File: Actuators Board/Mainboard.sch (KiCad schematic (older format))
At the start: 41 parts, among them J10 Conn_01x02_Male, J9 Conn_01x02_Male, Q1 MMDT2222A, U1 CP2102N-A01-GQFN24, U2 SN65HVD230, U3 ESP32-WROOM-32D

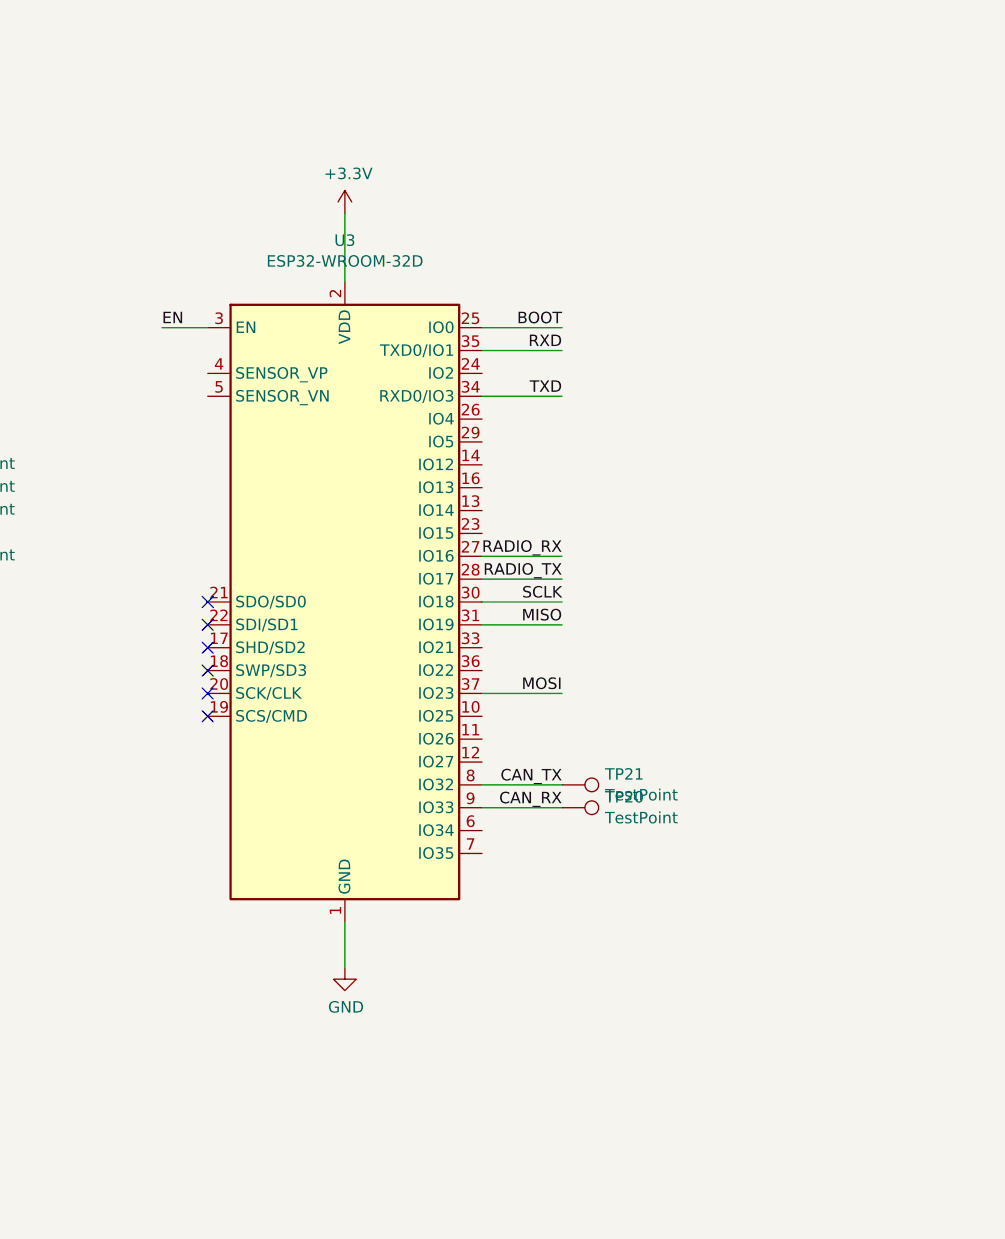
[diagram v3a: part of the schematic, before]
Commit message: pico swap done
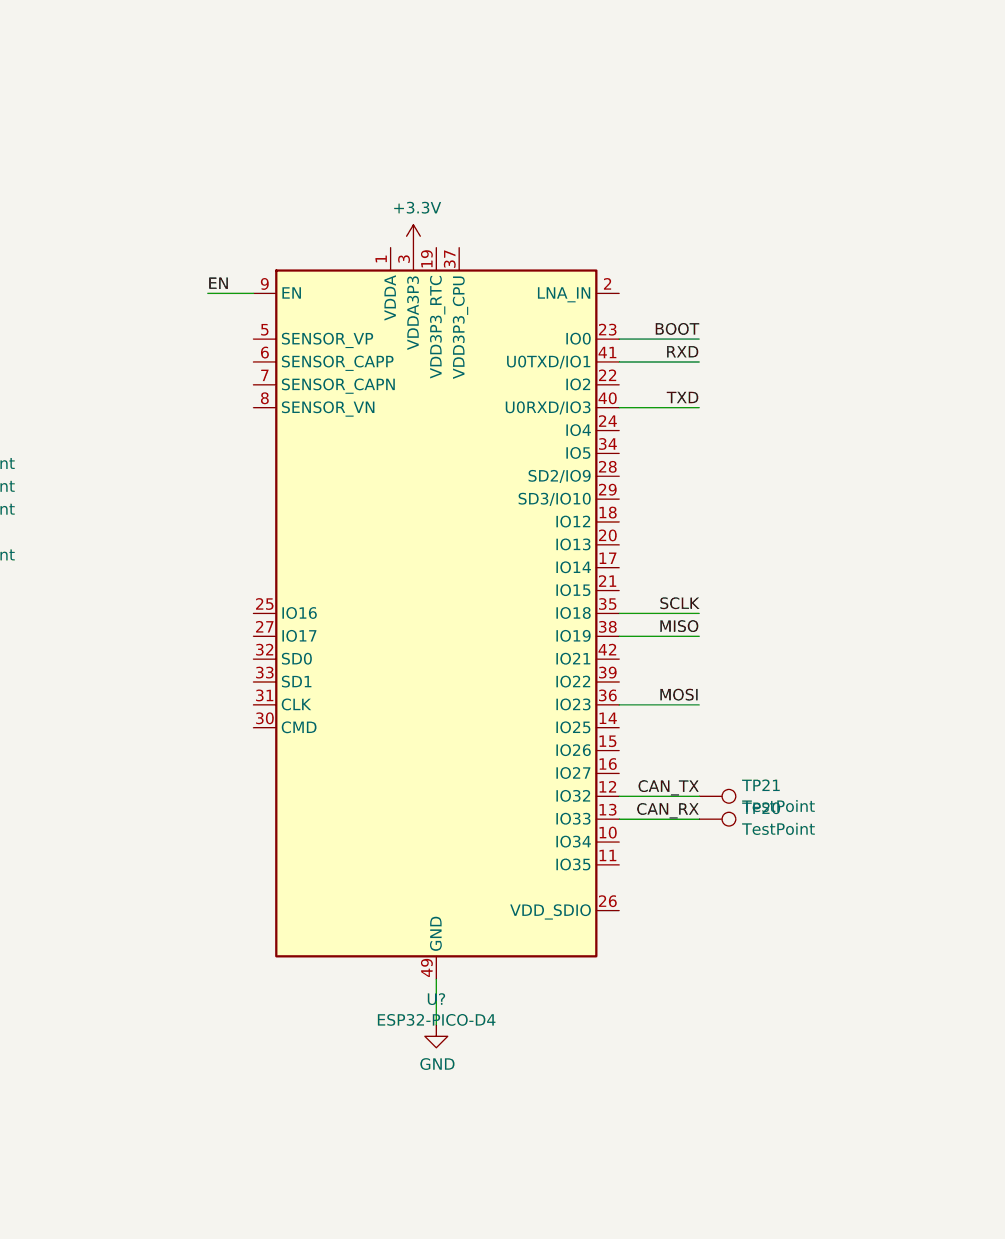
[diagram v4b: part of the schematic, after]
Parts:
- removed U3: ESP32-WROOM-32D, RF_Module:ESP32-WROOM-32, symbol RF_Module:ESP32-WROOM-32
- added U?: ESP32-PICO-D4, Package_DFN_QFN:QFN-48-1EP_7x7mm_P0.5mm_EP5.3x5.3mm, symbol RF_Module:ESP32-PICO-D4
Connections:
- net +3V3: now also U?.3 (VDDA3P3), U?.4 (VDDA3P3)
- net BOOT: now also U?.23 (IO0)
- net CAN_RX: now also U?.13 (IO33)
- net CAN_TX: now also U?.12 (IO32)
- net EN: now also U?.9 (EN)
- net GND: now also U?.49 (GND)
- net MISO: now also U?.38 (IO19)
- net MOSI: now also U?.36 (IO23)
- net RXD: now also U?.41 (U0TXD/IO1)
- net SCLK: now also U?.35 (IO18)
- net TXD: now also U?.40 (U0RXD/IO3)
- new net: U?.1 (VDDA), U?.43 (VDDA), U?.46 (VDDA)
- no-connect marks 19 -> 13
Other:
- moved on the sheet: TP20, TP21
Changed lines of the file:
@@
 L power:+3.3V #PWR020
 U 1 1 5DA60792
-P 6250 2050
-F 0 "#PWR020" H 6250 1900 50  0001 C CNN
-F 1 "+3.3V" H 6265 2223 50  0000 C CNN
-F 2 "" H 6250 2050 50  0001 C CNN
-F 3 "" H 6250 2050 50  0001 C CNN
-	1    6250 2050
-	1    0    0    -1
-$EndComp
-Wire Wire Line
-	6250 2050 6250 2350
+P 6550 2200
+F 0 "#PWR020" H 6550 2050 50  0001 C CNN
+F 1 "+3.3V" H 6565 2373 50  0000 C CNN
+F 2 "" H 6550 2200 50  0001 C CNN
+F 3 "" H 6550 2200 50  0001 C CNN
+	1    6550 2200
+	1    0    0    -1
+$EndComp
 $Comp
 L power:GND #PWR021
 U 1 1 5DA6110D
-P 6250 5350
-F 0 "#PWR021" H 6250 5100 50  0001 C CNN
-F 1 "GND" H 6255 5177 50  0000 C CNN
-F 2 "" H 6250 5350 50  0001 C CNN
-F 3 "" H 6250 5350 50  0001 C CNN
-	1    6250 5350
-	1    0    0    -1
-$EndComp
-Wire Wire Line
-	6250 5150 6250 5350
+P 6650 5600
+F 0 "#PWR021" H 6650 5350 50  0001 C CNN
+F 1 "GND" H 6655 5427 50  0000 C CNN
+F 2 "" H 6650 5600 50  0001 C CNN
+F 3 "" H 6650 5600 50  0001 C CNN
+	1    6650 5600
+	1    0    0    -1
+$EndComp
+Wire Wire Line
+	6650 5400 6650 5600
 $Comp
 L power:+3.3V #PWR06
@@
 Text Notes 10600 7700 0    50   ~ 0
 0.1\n\n
-Text Label 7200 3850 2    50   ~ 0
+Text Label 7800 3900 2    50   ~ 0
 MISO
-Text Label 7200 3750 2    50   ~ 0
+Text Label 7800 3800 2    50   ~ 0
 SCLK
-Wire Wire Line
-	5450 2550 5650 2550
-Text Label 5450 2550 0    50   ~ 0
-EN
 Text Label 1550 7550 2    50   ~ 0
 EN
-Text Label 7200 2550 2    50   ~ 0
+Text Label 7800 2600 2    50   ~ 0
 BOOT
 $Comp
@@
 TXD
 Wire Wire Line
-	6850 2550 7200 2550
-Wire Wire Line
-	6850 2650 7200 2650
-Wire Wire Line
-	6850 2850 7200 2850
-Wire Wire Line
-	6850 3750 7200 3750
-Wire Wire Line
-	6850 3850 7200 3850
-Wire Wire Line
-	6850 4150 7200 4150
+	7450 2600 7800 2600
+Wire Wire Line
+	7450 2700 7800 2700
+Wire Wire Line
+	7450 2900 7800 2900
+Wire Wire Line
+	7450 3800 7800 3800
+Wire Wire Line
+	7450 3900 7800 3900
+Wire Wire Line
+	7450 4200 7800 4200
 NoConn ~ 4000 3800
 NoConn ~ 4000 3900
@@
 Text Label 4300 3300 2    50   ~ 0
 TXD
-Text Label 7200 2650 2    50   ~ 0
+Text Label 7800 2700 2    50   ~ 0
 RXD
-Text Label 7200 2850 2    50   ~ 0
+Text Label 7800 2900 2    50   ~ 0
 TXD
 $Comp
@@
 	2200 2750 2400 2750
 Wire Wire Line
-	6850 3650 7200 3650
-Wire Wire Line
-	6850 3550 7200 3550
-Text Label 7200 3550 2    50   ~ 0
-RADIO_RX
-Text Label 7200 3650 2    50   ~ 0
-RADIO_TX
-$Comp
-L RF_Module:ESP32-WROOM-32 U3
-U 1 1 5DA5F4C7
-P 6250 3750
-F 0 "U3" H 6250 5331 50  0000 C CNN
-F 1 "ESP32-WROOM-32D" H 6250 5240 50  0000 C CNN
-F 2 "RF_Module:ESP32-WROOM-32" H 6250 2250 50  0001 C CNN
-F 3 "https://www.espressif.com/sites/default/files/documentation/esp32-wroom-32d_esp32-wroom-32u_datasheet_en.pdf" H 5950 3800 50  0001 C CNN
-	1    6250 3750
-	1    0    0    -1
-$EndComp
-Wire Wire Line
-	6850 4650 7200 4650
-Wire Wire Line
-	6850 4550 7200 4550
-Text Label 7200 4650 2    50   ~ 0
+	7450 4700 7800 4700
+Wire Wire Line
+	7450 4600 7800 4600
+Text Label 7800 4700 2    50   ~ 0
 CAN_RX
-Text Label 7200 4550 2    50   ~ 0
+Text Label 7800 4600 2    50   ~ 0
 CAN_TX
 Wire Wire Line
@@
 Wire Wire Line
 	3850 7050 4150 7050
-Text Label 7200 4150 2    50   ~ 0
+Text Label 7800 4200 2    50   ~ 0
 MOSI
 Wire Wire Line
@@
 L Connector:TestPoint TP20
 U 1 1 5DF4B310
-P 7200 4650
-F 0 "TP20" V 7154 4838 50  0000 L CNN
-F 1 "TestPoint" V 7245 4838 50  0000 L CNN
-F 2 "TestPoint:TestPoint_THTPad_1.0x1.0mm_Drill0.5mm" H 7400 4650 50  0001 C CNN
-F 3 "~" H 7400 4650 50  0001 C CNN
-	1    7200 4650
+P 7800 4700
+F 0 "TP20" V 7754 4888 50  0000 L CNN
+F 1 "TestPoint" V 7845 4888 50  0000 L CNN
+F 2 "TestPoint:TestPoint_THTPad_1.0x1.0mm_Drill0.5mm" H 8000 4700 50  0001 C CNN
+F 3 "~" H 8000 4700 50  0001 C CNN
+	1    7800 4700
 	0    1    1    0
 $EndComp
@@
 L Connector:TestPoint TP21
 U 1 1 5DF58E12
-P 7200 4550
-F 0 "TP21" V 7154 4738 50  0000 L CNN
-F 1 "TestPoint" V 7245 4738 50  0000 L CNN
-F 2 "TestPoint:TestPoint_THTPad_1.0x1.0mm_Drill0.5mm" H 7400 4550 50  0001 C CNN
-F 3 "~" H 7400 4550 50  0001 C CNN
-	1    7200 4550
-	0    1    1    0
-$EndComp
-NoConn ~ 5650 3750
-NoConn ~ 5650 3850
-NoConn ~ 5650 3950
-NoConn ~ 5650 4050
-NoConn ~ 5650 4150
-NoConn ~ 5650 4250
+P 7800 4600
+F 0 "TP21" V 7754 4788 50  0000 L CNN
+F 1 "TestPoint" V 7845 4788 50  0000 L CNN
+F 2 "TestPoint:TestPoint_THTPad_1.0x1.0mm_Drill0.5mm" H 8000 4600 50  0001 C CNN
+F 3 "~" H 8000 4600 50  0001 C CNN
+	1    7800 4600
+	0    1    1    0
+$EndComp
 $Comp
 L Transistor_BJT:MMDT2222A Q1
@@
 	2000 2950 2000 3050
 Connection ~ 2000 3050
+$Comp
+L RF_Module:ESP32-PICO-D4 U?
+U 1 1 618B08BE
+P 6650 3800
+F 0 "U?" H 6650 2111 50  0000 C CNN
+F 1 "ESP32-PICO-D4" H 6650 2020 50  0000 C CNN
+F 2 "Package_DFN_QFN:QFN-48-1EP_7x7mm_P0.5mm_EP5.3x5.3mm" H 6650 2100 50  0001 C CNN
+F 3 "https://www.espressif.com/sites/default/files/documentation/esp32-pico-d4_datasheet_en.pdf" H 6900 2800 50  0001 C CNN
+	1    6650 3800
+	1    0    0    -1
+$EndComp
+Text Label 5650 2400 0    50   ~ 0
+EN
+Wire Wire Line
+	5650 2400 5850 2400
 $EndSCHEMATC
